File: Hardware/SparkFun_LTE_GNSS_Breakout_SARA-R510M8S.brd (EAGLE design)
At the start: 76.2 x 50.8 mm, 254 parts, among them IC1 SN74AVC4T774PW, IC2 SN74AVC4T774PW, J13 TP, J17 NANO_SIM, J19 NI, Q1 310mA/60V/1.6Ω, Q2 310mA/60V/1.6Ω, Q3 310mA/60V/1.6Ω, Q4 310mA/60V/1.6Ω, Q5 20V/0.2A/8MHz/1.2Ω/1Vth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

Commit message: V10
Added 100k Pulldown resistors to RTS and DTR
Moved "L1" label from the top of the board to the bottom
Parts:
- added R17, R19: 100k, SparkFun-Resistors:0603
- moved C6 2.29 mm to (30.6, 10.9)
- moved R2 1.66 mm to (30.6, 9.27)
- moved U$42 0.76 mm to (67.8, 47.4), flipped to the bottom
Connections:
- net DTR: now also R17.2
- net GND: now also R17.1, R19.1
- net RTS: now also R19.2
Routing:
- net DTR: track 35.6 -> 48.8 mm
- net RTS: track 15.8 -> 27.0 mm
- net SARA_ON: track 51.2 -> 53.3 mm
- net GND: track 27.0 -> 28.4 mm
- net N$10: track 9.96 -> 9.26 mm
- net 3.3V: track 91.7 -> 91.1 mm
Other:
- board text added: "V10"
- board text removed: "V01"

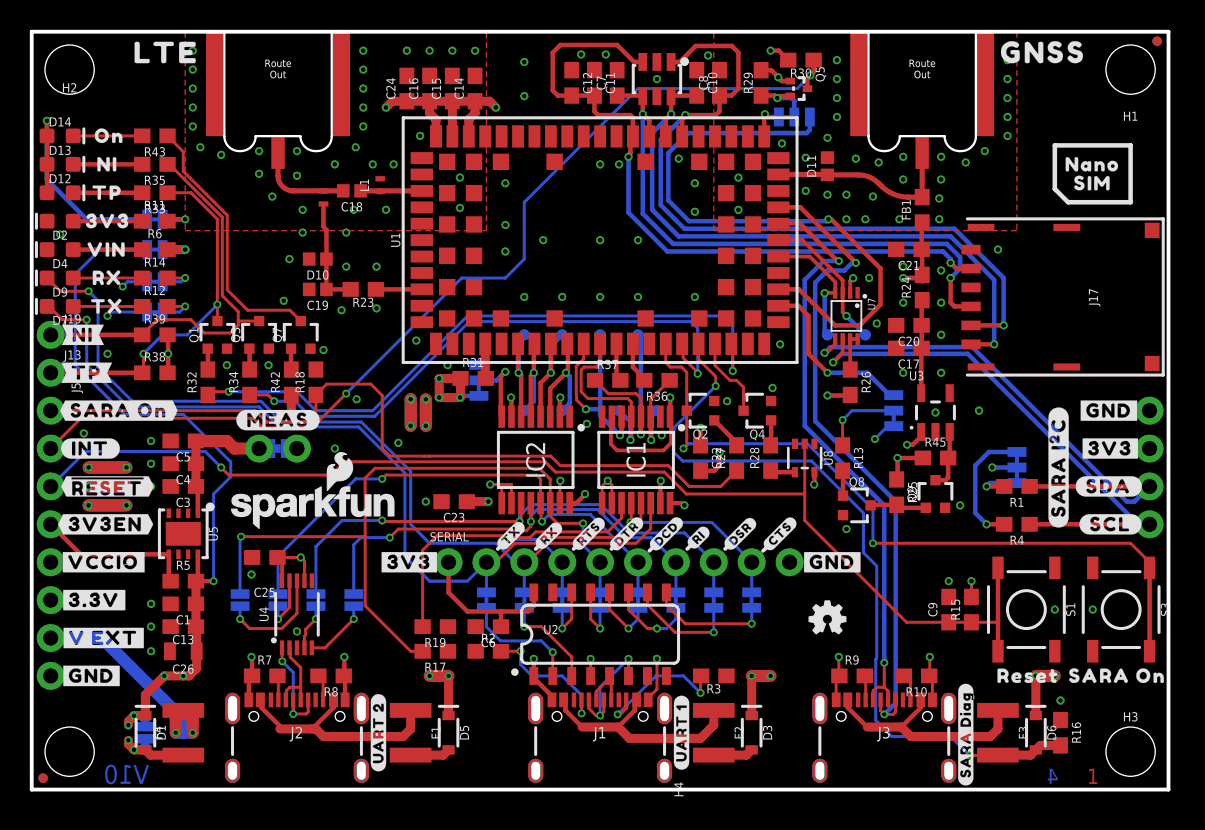
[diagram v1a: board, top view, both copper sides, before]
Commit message: V10 design review changes
-Updated Schematic PDF
-Added new parts to sparkfun libraries
-Fixed labels for schematic sections
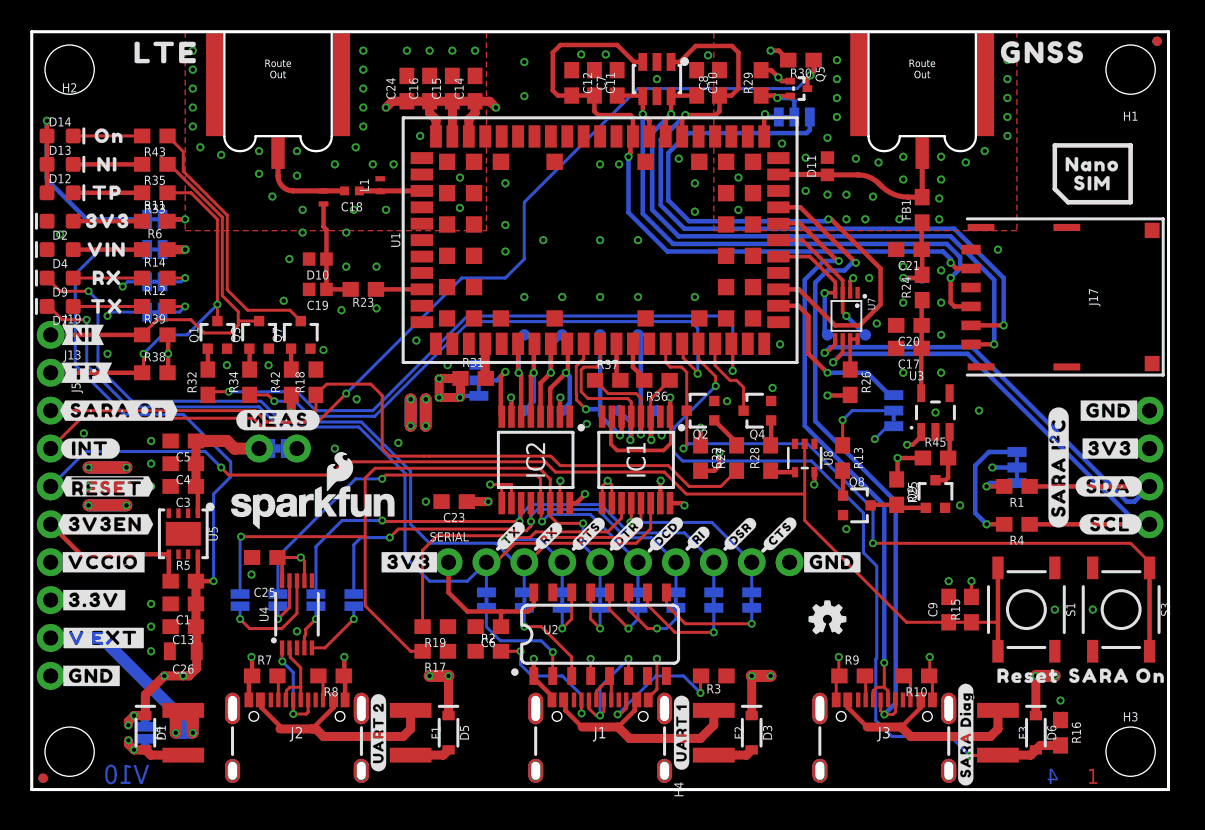
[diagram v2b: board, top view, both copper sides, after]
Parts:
- C18: device New_Parts:0402 -> SparkFun-Capacitors:0402-TIGHT
- C19: device New_Parts:0402 -> SparkFun-Capacitors:0402
- D10, D11: device New_Parts:0402 -> SparkFun-DiscreteSemi:0402
- IC1, IC2: device New_Parts:SOP65P640X120-16N -> SparkFun-IC-Comms:SOP65P640X120-16N
- L1, L2: device New_Parts:0402_COILCRAFT -> SparkFun-Coils:0402_COILCRAFT
- U1: device SARA_R5:SARA-LGA -> SparkFun-RF:SARA-LGA
